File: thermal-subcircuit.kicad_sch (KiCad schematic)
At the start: 15 parts, among them Q1 SQ3461EV, U2 TLV1805-Q1DBV, U3 TS5A3159-Q1

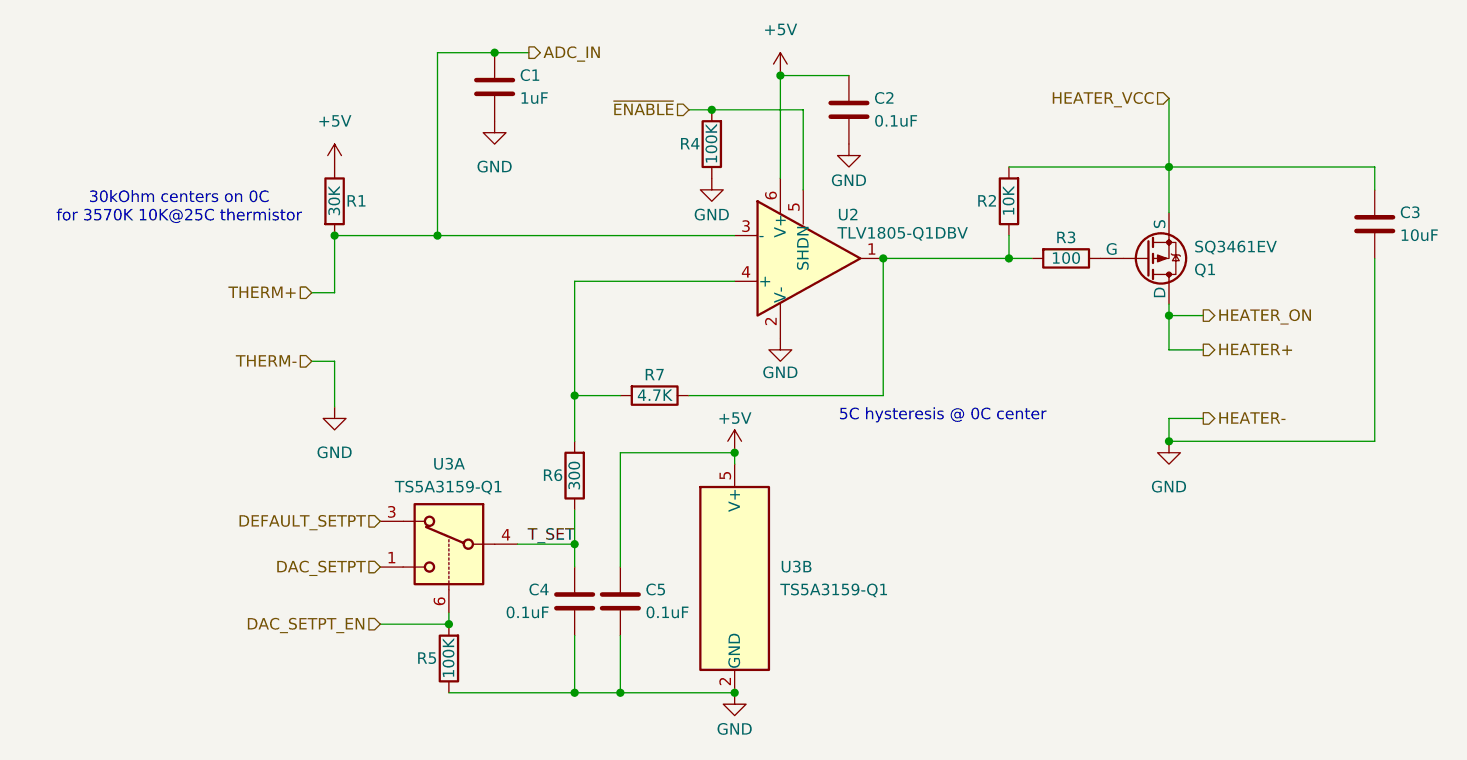
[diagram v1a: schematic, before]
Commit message: dpt sheet and move thermals into subsheet
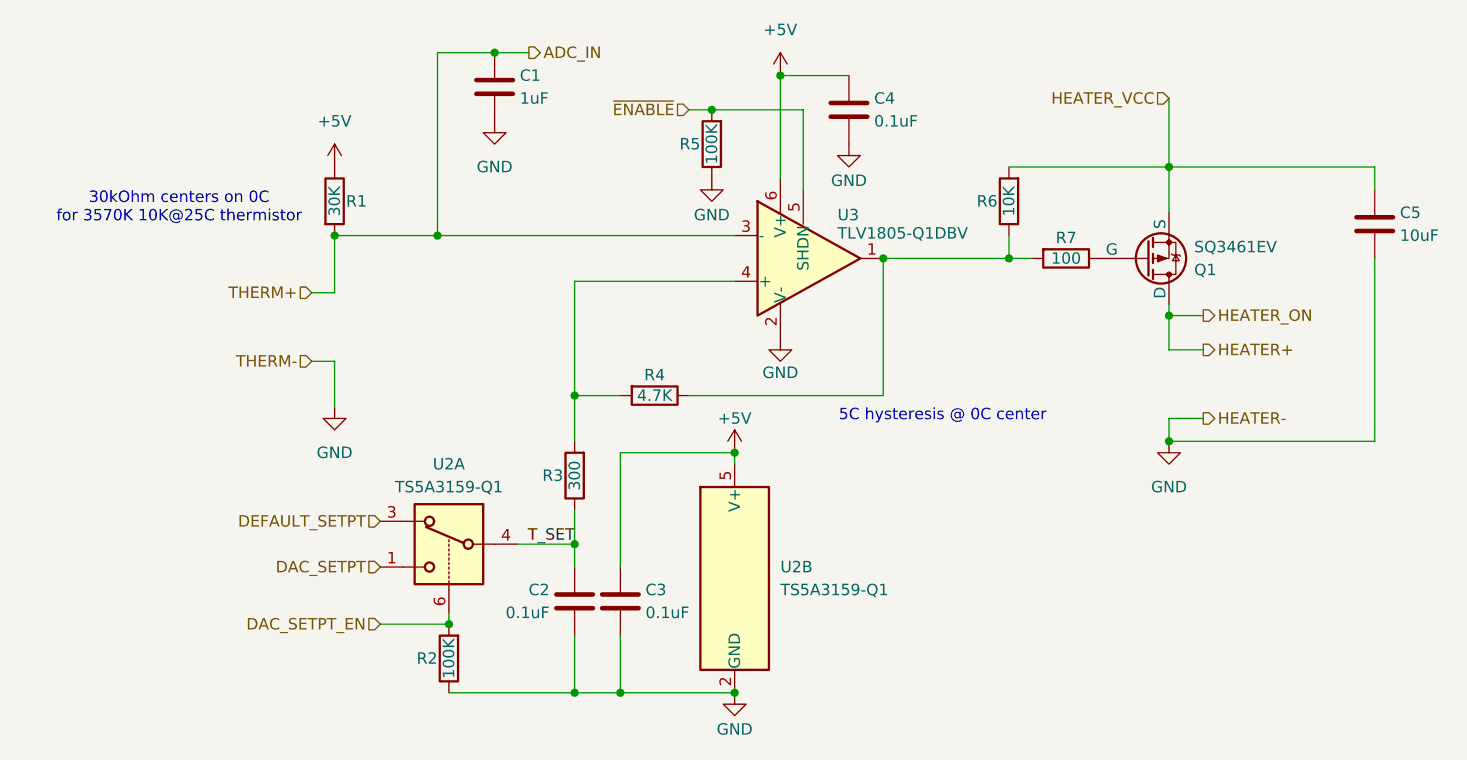
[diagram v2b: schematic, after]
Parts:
- renumbered C4 to C2, C5 to C3, C2 to C4, C3 to C5, R5 to R2, R6 to R3, R7 to R4, R4 to R5, R2 to R6, R3 to R7, U3 to U2, U2 to U3

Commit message: syms
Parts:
- added R251: 10K, symbol Device:R
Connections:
- net DAC_SETPT_EN: now also R2.1; no longer R2.2
- net GND: now also R2.2; no longer R2.1
- net HEATER+: now also R251.1
- net ADC_IN renamed THERM+
- new net HEATER_ON: R251.2
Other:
- moved on the sheet: R2

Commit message: midnight work
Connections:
- net +5V: no longer R1.1
- new net THERMISTOR_SUP: R1.1
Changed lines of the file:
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@@
+	(wire
+		(pts
+			(xy 53.34 58.42) (xy 53.34 62.23)
+		)
+		(stroke
+			(width 0)
+			(type default)
+		)
+	)
 	(wire
 		(pts
@@
 			)
 			(justify right bottom)
+		)
+	)
+	(global_label "THERMISTOR_SUP"
+		(shape input)
+		(at 53.34 58.42 180)
+		(fields_autoplaced yes)
+		(effects
+			(font
+				(size 1.27 1.27)
+			)
+			(justify right)
+		)
+		(property "Intersheetrefs" "${INTERSHEET_REFS}"
+			(at 34.0263 58.42 0)
+			(effects
+				(font
+					(size 1.27 1.27)
+				)
+				(justify right)
+				(hide yes)
+			)
 		)
 	)
@@
 					(unit 1)
 				)
-			)
-		)
-	)
-	(symbol
-		(lib_id "power:+5V")
-		(at 53.34 62.23 0)
-		(unit 1)
-		(exclude_from_sim no)
-		(in_bom yes)
-		(on_board yes)
-		(dnp no)
-		(fields_autoplaced yes)
-		(property "Reference" "#PWR01"
-			(at 53.34 66.04 0)
-			(effects
-				(font
-					(size 1.27 1.27)
-				)
-				(hide yes)
-			)
-		)
-		(property "Value" "+5V"
-			(at 53.34 57.15 0)
-			(effects
-				(font
-					(size 1.27 1.27)
-				)
-			)
-		)
-		(property "Footprint" ""
-			(at 53.34 62.23 0)
-			(effects
-				(font
-					(size 1.27 1.27)
-				)
-				(hide yes)
-			)
-		)
-		(property "Datasheet" ""
-			(at 53.34 62.23 0)
-			(effects
-				(font
-					(size 1.27 1.27)
-				)
-				(hide yes)
-			)
-		)
-		(property "Description" "Power symbol creates a global label with name \"+5V\""
-			(at 53.34 62.23 0)
-			(effects
-				(font
-					(size 1.27 1.27)
-				)
-				(hide yes)
-			)
-		)
-		(pin "1"
-		)
-		(instances
-			(project "femta-control"
-				(path "/838bf11c-36b7-41d7-9462-fe98a188d617/217e6ea2-6933-4a2a-93ca-61414ae3305a/c29214a2-445b-49c4-ba25-1140c8e459b9"
-					(reference "#PWR01")
-					(unit 1)
-				)
-				(path "/838bf11c-36b7-41d7-9462-fe98a188d617/217e6ea2-6933-4a2a-93ca-61414ae3305a/b1c59384-d247-4ca3-8131-32a43effa82e"
-					(reference "#PWR016")
-					(unit 1)
-				)
-				(path "/838bf11c-36b7-41d7-9462-fe98a188d617/217e6ea2-6933-4a2a-93ca-61414ae3305a/b4cc5372-aa01-49d6-a2cf-514598e33d47"
-					(reference "#PWR011")
-					(unit 1)
-				)
-				(path "/838bf11c-36b7-41d7-9462-fe98a188d617/217e6ea2-6933-4a2a-93ca-61414ae3305a/88a1aa13-44ed-4ade-abb2-7a4c1d117491"
-					(reference "#PWR050")
-					(unit 1)
-				)
-				(path "/838bf11c-36b7-41d7-9462-fe98a188d617/217e6ea2-6933-4a2a-93ca-61414ae3305a/a216897b-af2d-4140-b7c1-52adc3cfb616"
-					(reference "#PWR060")
-					(unit 1)
-				)
-				(path "/838bf11c-36b7-41d7-9462-fe98a188d617/217e6ea2-6933-4a2a-93ca-61414ae3305a/ca534e7a-556e-4ed2-9442-39dd3e4c8cf2"
-					(reference "#PWR070")
-					(unit 1)
-				)
-				(path "/838bf11c-36b7-41d7-9462-fe98a188d617/217e6ea2-6933-4a2a-93ca-61414ae3305a/8dc5561c-b341-482e-9dda-d5dcaa4d2154"
-					(reference "#PWR080")
-					(unit 1)
-				)
-				(path "/838bf11c-36b7-41d7-9462-fe98a188d617/217e6ea2-6933-4a2a-93ca-61414ae3305a/3b4c0847-39c3-4219-942c-72f9d54dec4a"
-					(reference "#PWR090")
-					(unit 1)
-				)
-				(path "/838bf11c-36b7-41d7-9462-fe98a188d617/217e6ea2-6933-4a2a-93ca-61414ae3305a/3d3d3c9e-3e53-4e6f-8fee-8374db12bea2"
-					(reference "#PWR0100")
-					(unit 1)
-				)
-				(path "/838bf11c-36b7-41d7-9462-fe98a188d617/217e6ea2-6933-4a2a-93ca-61414ae3305a/e3b97ebd-98e5-4095-95e3-eeadaa7cf18f"
-					(reference "#PWR0110")
-					(unit 1)
-				)
-				(path "/838bf11c-36b7-41d7-9462-fe98a188d617/217e6ea2-6933-4a2a-93ca-61414ae3305a/0c62f644-f5eb-458e-aeef-bad21e641cf5"
-					(reference "#PWR0120")
-					(unit 1)
-				)
-				(path "/838bf11c-36b7-41d7-9462-fe98a188d617/217e6ea2-6933-4a2a-93ca-61414ae3305a/efb6f2ad-ed1b-45aa-9efc-77ea10a58a56"
-					(reference "#PWR0130")
-					(unit 1)
-				)
-				(path "/838bf11c-36b7-41d7-9462-fe98a188d617/217e6ea2-6933-4a2a-93ca-61414ae3305a/32e22e35-b33b-47a1-a6d3-56fb349a24b3"
-					(reference "#PWR0139")
-					(unit 1)
-				)
-				(path "/838bf11c-36b7-41d7-9462-fe98a188d617/217e6ea2-6933-4a2a-93ca-61414ae3305a/e6090e5c-2de4-4cd4-ac65-2ae4c3f701d2"
-					(reference "#PWR0150")
-					(unit 1)
-				)
-				(path "/838bf11c-36b7-41d7-9462-fe98a188d617/217e6ea2-6933-4a2a-93ca-61414ae3305a/77aca0ba-9663-408a-a914-f8ed5f8f9425"
-					(reference "#PWR0160")
-					(unit 1)
-				)
-				(path "/838bf11c-36b7-41d7-9462-fe98a188d617/217e6ea2-6933-4a2a-93ca-61414ae3305a/11754e5e-c30d-4884-9c92-3bdd3836ddd5"
-					(reference "#PWR0170")
-					(unit 1)
-				)
